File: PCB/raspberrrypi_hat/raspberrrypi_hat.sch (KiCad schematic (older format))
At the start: 18 parts, among them J1 40HAT, J2 CONN_02X02, J3 CONN_01X02, Q1 DMG2305UX, Q2 DMMT5401, U1 CAT24C32

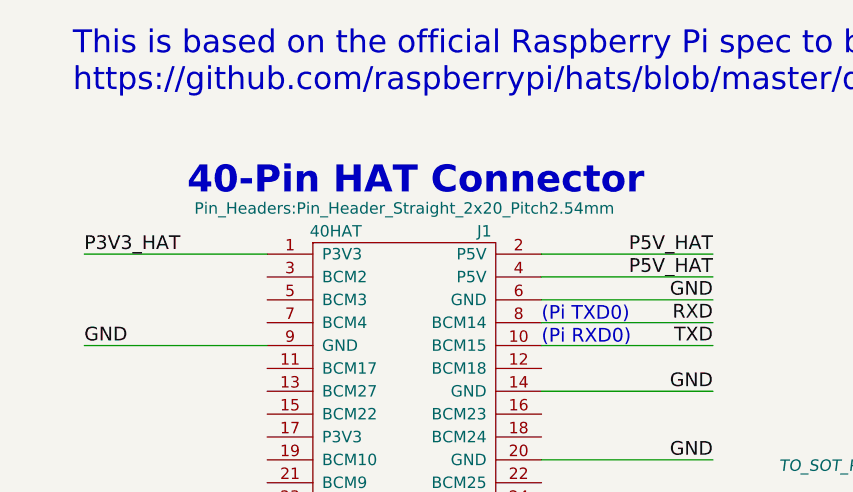
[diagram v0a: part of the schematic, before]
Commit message: Fix #7 Wrong GPIO header footprint
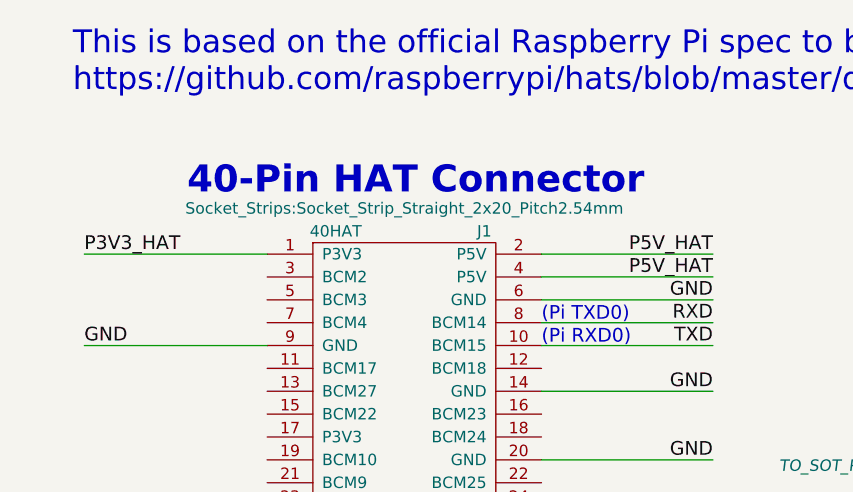
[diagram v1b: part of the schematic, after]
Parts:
- J1: footprint Pin_Headers:Pin_Header_Straight_2x20_Pitch2.54mm -> Socket_Strips:Socket_Strip_Straight_2x20_Pitch2.54mm
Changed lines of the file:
@@
 F 0 "J1" H 2450 1700 50  0000 C CNN
 F 1 "40HAT" H 1800 1700 50  0000 C CNN
-F 2 "Pin_Headers:Pin_Header_Straight_2x20_Pitch2.54mm" H 2100 1800 50  0000 C CNN
+F 2 "Socket_Strips:Socket_Strip_Straight_2x20_Pitch2.54mm" H 2100 1800 50  0000 C CNN
 F 3 "" H 1400 1600 50  0000 C CNN
 	1    2100 1600
